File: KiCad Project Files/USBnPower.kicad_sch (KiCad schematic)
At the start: 11 parts, among them J1 SM04B, U3 XC6206PxxxMR, U4 PRTR5V0U2X

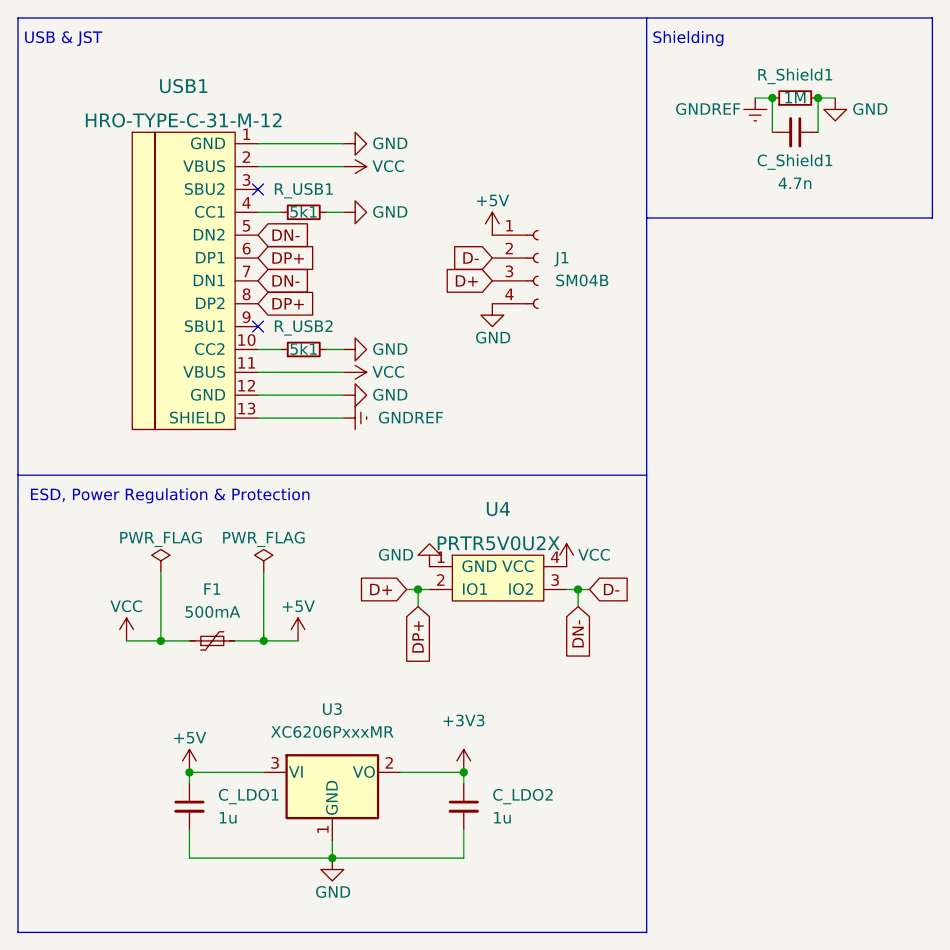
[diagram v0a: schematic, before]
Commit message: Initial Modifications
Summary of changes from original SST60:
-Removes extraneous keys, opting for ANSI-only, split right shift, split Backspace, 7U space bar, stepped caps lock.
-Switched from MX-ANSI hybrid to MX-only
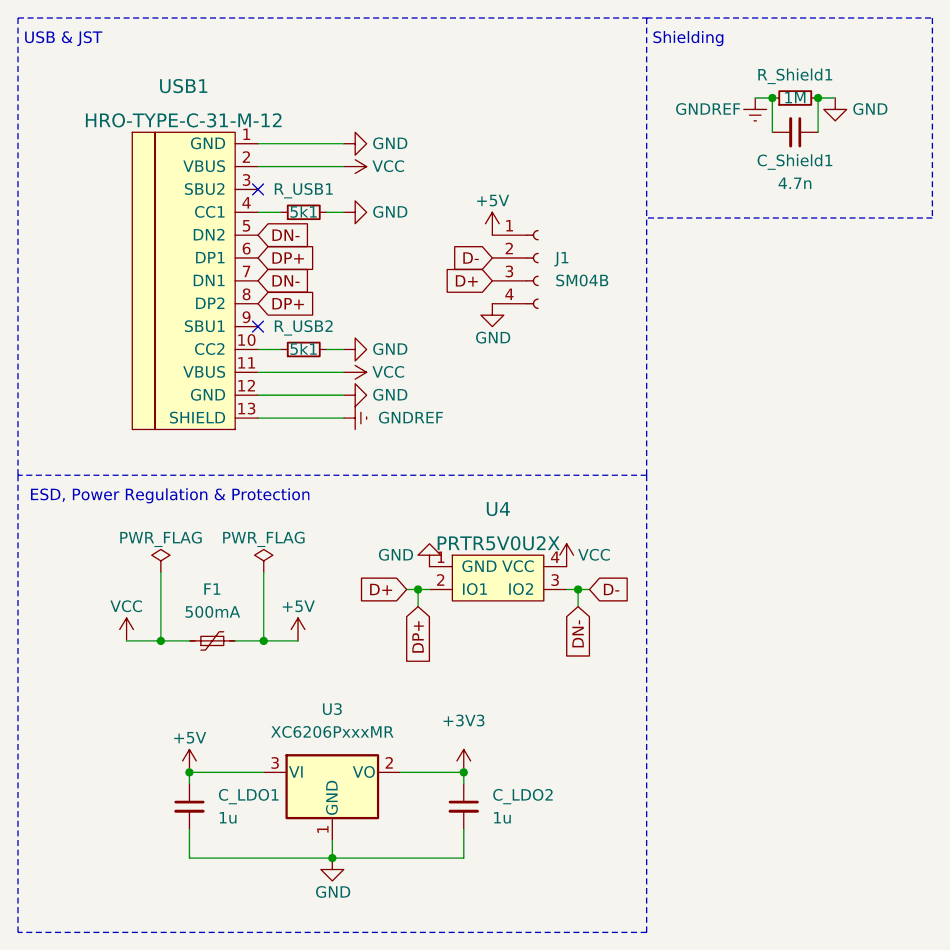
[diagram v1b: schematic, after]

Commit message: Error Cleanup
Resolved all errors in sch, and most errors in pcb, except "intentional" ones concerning H1.
Will readdress rule changes and violations once attempting to submit to fab house.
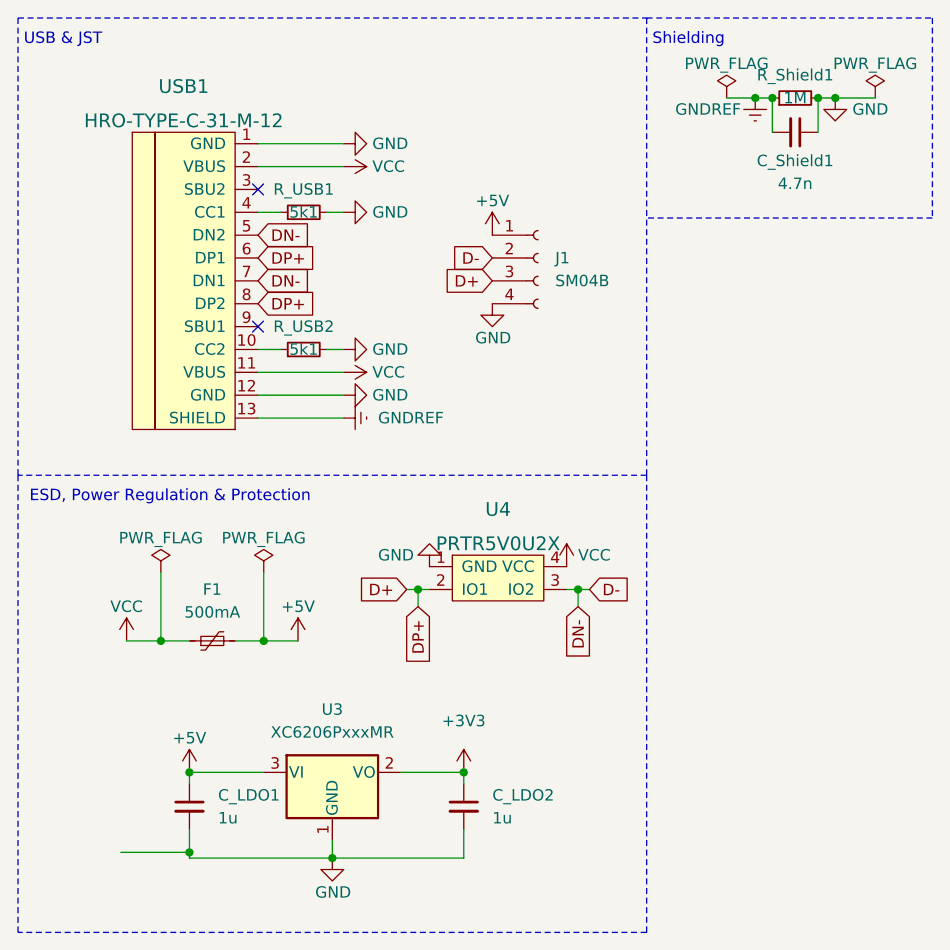
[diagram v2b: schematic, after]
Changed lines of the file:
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@@
+	)
+	(junction
+		(at 94.615 21.59)
+		(diameter 0)
+		(color 0 0 0 0)
 	)
 	(junction
@@
 	)
 	(junction
+		(at 103.505 21.59)
+		(diameter 0)
+		(color 0 0 0 0)
+	)
+	(junction
+		(at 31.75 105.41)
+		(diameter 0)
+		(color 0 0 0 0)
+	)
+	(junction
 		(at 28.575 81.915)
 		(diameter 0)
@@
 	(wire
 		(pts
+			(xy 103.505 21.59) (xy 107.95 21.59)
+		)
+		(stroke
+			(width 0)
+			(type default)
+		)
+	)
+	(wire
+		(pts
 			(xy 57.15 76.2) (xy 58.42 76.2)
 		)
@@
 	(wire
 		(pts
-			(xy 31.75 102.87) (xy 31.75 106.045)
+			(xy 31.75 102.87) (xy 31.75 105.41)
 		)
 		(stroke
@@
 		)
 	)
+	(wire
+		(pts
+			(xy 24.13 105.41) (xy 31.75 105.41)
+		)
+		(stroke
+			(width 0)
+			(type default)
+		)
+	)
 	(polyline
 		(pts
@@
 	(wire
 		(pts
+			(xy 91.44 21.59) (xy 94.615 21.59)
+		)
+		(stroke
+			(width 0)
+			(type default)
+		)
+	)
+	(wire
+		(pts
+			(xy 28.575 74.295) (xy 28.575 81.915)
+		)
+		(stroke
+			(width 0)
+			(type default)
+		)
+	)
+	(wire
+		(pts
+			(xy 74.93 76.2) (xy 76.2 76.2)
+		)
+		(stroke
+			(width 0)
+			(type default)
+		)
+	)
+	(wire
+		(pts
+			(xy 39.37 29.21) (xy 48.895 29.21)
+		)
+		(stroke
+			(width 0)
+			(type default)
+		)
+	)
+	(wire
+		(pts
+			(xy 62.23 96.52) (xy 62.23 97.79)
+		)
+		(stroke
+			(width 0)
+			(type default)
+		)
+	)
+	(polyline
+		(pts
+			(xy 114.3 34.925) (xy 82.55 34.925)
+		)
+		(stroke
+			(width 0)
+			(type dash)
+		)
+	)
+	(wire
+		(pts
 			(xy 94.615 21.59) (xy 96.52 21.59)
 		)
@@
 		)
 	)
-	(wire
-		(pts
-			(xy 28.575 74.295) (xy 28.575 81.915)
-		)
-		(stroke
-			(width 0)
-			(type default)
-		)
-	)
-	(wire
-		(pts
-			(xy 74.93 76.2) (xy 76.2 76.2)
-		)
-		(stroke
-			(width 0)
-			(type default)
-		)
-	)
-	(wire
-		(pts
-			(xy 39.37 29.21) (xy 48.895 29.21)
-		)
-		(stroke
-			(width 0)
-			(type default)
-		)
-	)
-	(wire
-		(pts
-			(xy 62.23 96.52) (xy 62.23 97.79)
-		)
-		(stroke
-			(width 0)
-			(type default)
-		)
-	)
 	(polyline
 		(pts
-			(xy 114.3 34.925) (xy 82.55 34.925)
+			(xy 12.7 12.7) (xy 82.55 12.7)
 		)
 		(stroke
@@
 		)
 	)
+	(wire
+		(pts
+			(xy 39.37 54.61) (xy 48.895 54.61)
+		)
+		(stroke
+			(width 0)
+			(type default)
+		)
+	)
+	(wire
+		(pts
+			(xy 57.15 76.2) (xy 57.15 78.105)
+		)
+		(stroke
+			(width 0)
+			(type default)
+		)
+	)
 	(polyline
 		(pts
-			(xy 12.7 12.7) (xy 82.55 12.7)
+			(xy 82.55 12.7) (xy 114.3 12.7)
 		)
 		(stroke
@@
 	(wire
 		(pts
-			(xy 39.37 54.61) (xy 48.895 54.61)
-		)
-		(stroke
-			(width 0)
-			(type default)
-		)
-	)
-	(wire
-		(pts
-			(xy 57.15 76.2) (xy 57.15 78.105)
-		)
-		(stroke
-			(width 0)
-			(type default)
-		)
-	)
-	(polyline
-		(pts
-			(xy 82.55 12.7) (xy 114.3 12.7)
-		)
-		(stroke
-			(width 0)
-			(type dash)
-		)
-	)
-	(wire
-		(pts
 			(xy 31.75 106.045) (xy 47.625 106.045)
 		)
@@
 		(pts
 			(xy 55.88 76.2) (xy 57.15 76.2)
+		)
+		(stroke
+			(width 0)
+			(type default)
+		)
+	)
+	(wire
+		(pts
+			(xy 31.75 105.41) (xy 31.75 106.045)
 		)
 		(stroke
@@
 	)
 	(symbol
+		(lib_id "power:PWR_FLAG")
+		(at 107.95 21.59 0)
+		(mirror y)
+		(unit 1)
+		(exclude_from_sim no)
+		(in_bom yes)
+		(on_board yes)
+		(dnp no)
+		(property "Reference" "#FLG01"
+			(at 107.95 19.685 0)
+			(effects
+				(font
+					(size 1.27 1.27)
+				)
+				(hide yes)
+			)
+		)
+		(property "Value" "PWR_FLAG"
+			(at 107.95 17.78 0)
+			(effects
+				(font
+					(size 1.27 1.27)
+				)
+			)
+		)
+		(property "Footprint" ""
+			(at 107.95 21.59 0)
+			(effects
+				(font
+					(size 1.27 1.27)
+				)
+				(hide yes)
+			)
+		)
+		(property "Datasheet" "~"
+			(at 107.95 21.59 0)
+			(effects
+				(font
+					(size 1.27 1.27)
+				)
+				(hide yes)
+			)
+		)
+		(property "Description" ""
+			(at 107.95 21.59 0)
+			(effects
+				(font
+					(size 1.27 1.27)
+				)
+				(hide yes)
+			)
+		)
+		(pin "1"
+		)
+		(instances
+			(project "SST60"
+				(path "/e63e39d7-6ac0-4ffd-8aa3-1841a4541b55/9e40d895-a947-4b33-a248-0d0dda788e56"
+					(reference "#FLG01")
+					(unit 1)
+				)
+			)
+		)
+	)
+	(symbol
 		(lib_id "power:GND")
 		(at 48.895 54.61 90)
@@
 	)
 	(symbol
+		(lib_id "power:PWR_FLAG")
+		(at 91.44 21.59 0)
+		(mirror y)
+		(unit 1)
+		(exclude_from_sim no)
+		(in_bom yes)
+		(on_board yes)
+		(dnp no)
+		(property "Reference" "#FLG02"
+			(at 91.44 19.685 0)
+			(effects
+				(font
+					(size 1.27 1.27)
+				)
+				(hide yes)
+			)
+		)
+		(property "Value" "PWR_FLAG"
+			(at 91.44 17.78 0)
+			(effects
+				(font
+					(size 1.27 1.27)
+				)
+			)
+		)
+		(property "Footprint" ""
+			(at 91.44 21.59 0)
+			(effects
+				(font
+					(size 1.27 1.27)
+				)
+				(hide yes)
+			)
+		)
+		(property "Datasheet" "~"
+			(at 91.44 21.59 0)
+			(effects
+				(font
+					(size 1.27 1.27)
+				)
+				(hide yes)
+			)
+		)
+		(property "Description" ""
+			(at 91.44 21.59 0)
+			(effects
+				(font
+					(size 1.27 1.27)
+				)
+				(hide yes)
+			)
+		)
+		(pin "1"
+		)
+		(instances
+			(project "SST60"
+				(path "/e63e39d7-6ac0-4ffd-8aa3-1841a4541b55/9e40d895-a947-4b33-a248-0d0dda788e56"
+					(reference "#FLG02")
+					(unit 1)
+				)
+			)
+		)
+	)
+	(symbol
 		(lib_id "power:GND")
 		(at 48.895 49.53 90)
@@
 		(on_board yes)
 		(dnp no)
-		(fields_autoplaced yes)
 		(property "Reference" "#PWR0131"
 			(at 103.505 27.94 0)

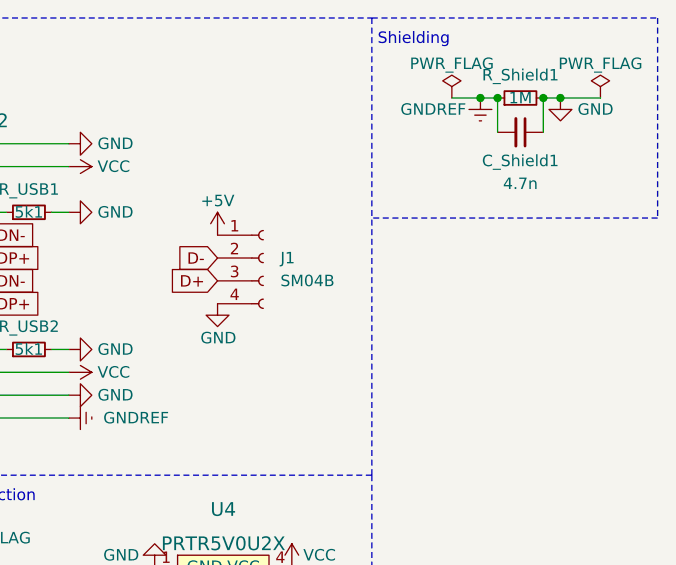
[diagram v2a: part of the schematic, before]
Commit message: Further Component Updates
More updating of components to decide what is and isn't included in output BOM and Placement files, as well as other component values, to smooth out wrinkles with JLC PCB process.
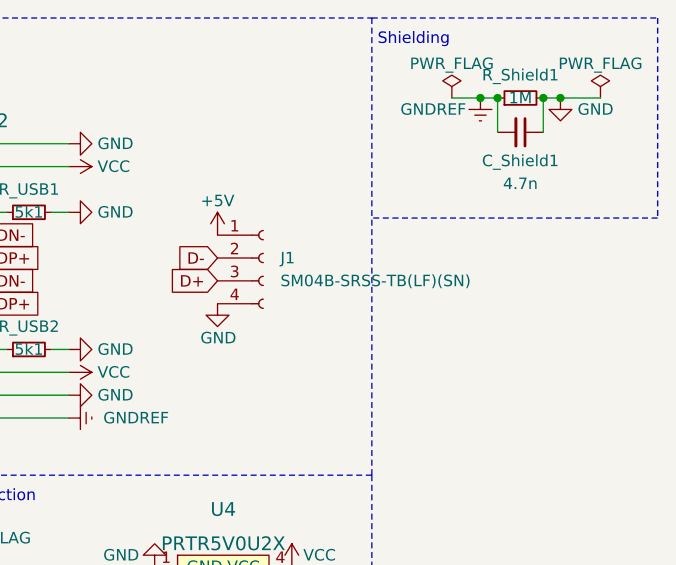
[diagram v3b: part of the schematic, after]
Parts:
- J1: value SM04B -> SM04B-SRSS-TB(LF)(SN)
- R_USB1, R_USB2, USB1: now left out of the parts list
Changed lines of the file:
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@@
 		(unit 1)
 		(exclude_from_sim no)
-		(in_bom yes)
+		(in_bom no)
 		(on_board yes)
 		(dnp no)
@@
 		(unit 1)
 		(exclude_from_sim no)
-		(in_bom yes)
+		(in_bom no)
 		(on_board yes)
 		(dnp no)
@@
 			)
 		)
-		(property "Value" "SM04B"
+		(property "Value" "SM04B-SRSS-TB(LF)(SN)"
 			(at 72.39 41.9099 0)
 			(effects
@@
 		(unit 1)
 		(exclude_from_sim no)
-		(in_bom yes)
-		(on_board yes)
-		(dnp no)
+		(in_bom no)
+		(on_board yes)
+		(dnp no)
